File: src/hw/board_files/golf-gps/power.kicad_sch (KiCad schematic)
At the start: 19 parts, among them J3 USB_C_Receptacle_PowerOnly_6P, SW1 SW_SPDT, U2 MCP73831-2-OT, U3 TPS63031DSKR

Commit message: Added BOM file, finishing sch
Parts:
- added F1: 500mA, symbol Device:Fuse_Small
- renumbered C14 to C4, C15 to C5, C5 to C6, C6 to C7, C7 to C8, C1 to C9, D3 to D2, R7 to R5, R8 to R6, R9 to R7, R10 to R8
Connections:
- net VBAT: now also BT2.1 (+), F1.1
- net V_BCKP: now reaches D1.3 (A)
- net V_LiPo: no longer names the net of SW1.1 (B)
- net V_LiPo: now also F1.2; no longer BT2.1 (+)
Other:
- note added: "LiPo Battery Charger"
- note added: "Power"
- note removed: "Add fuse"
- note removed: "LiPo Charger"
- company: (none) -> Brady Kuhn
- title: (none) -> Golf GPS
- moved on the sheet: BT1, BT2, C4, C5, C6, C7, C8, C9, D1, D2, J3, L1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

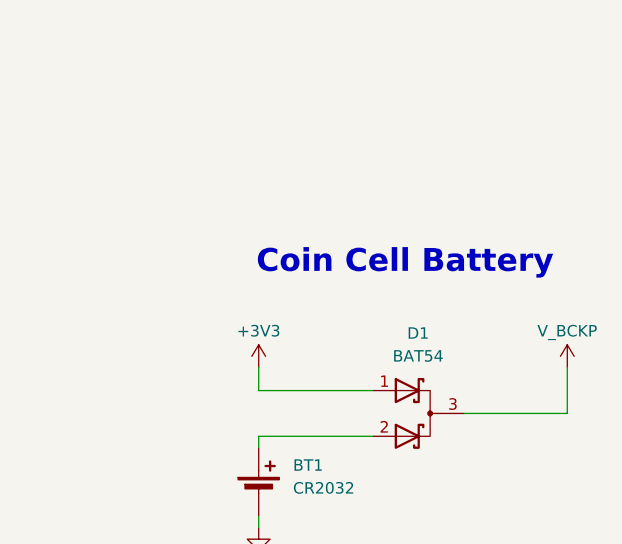
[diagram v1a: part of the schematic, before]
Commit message: Added PI filter to antenna.
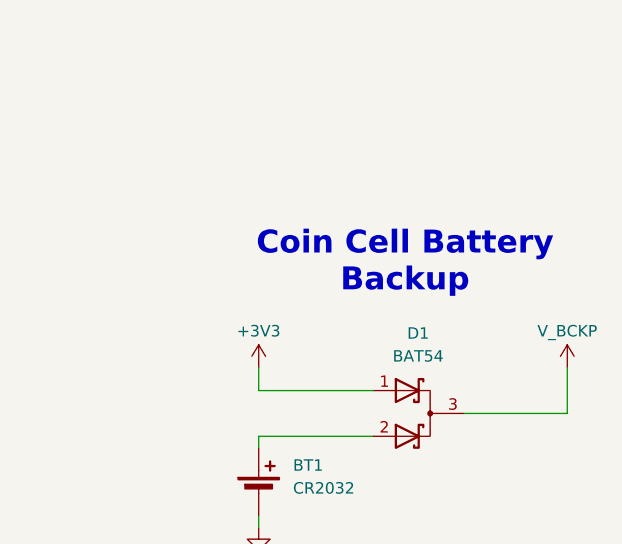
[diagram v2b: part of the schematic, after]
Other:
- note added: "Coin Cell Battery Backup"
- note removed: "Coin Cell Battery"
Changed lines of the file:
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@@
 		)
 	)
-	(text "Coin Cell Battery"
+	(text "Coin Cell Battery\nBackup"
 		(exclude_from_sim no)
 		(at 214.376 40.386 0)

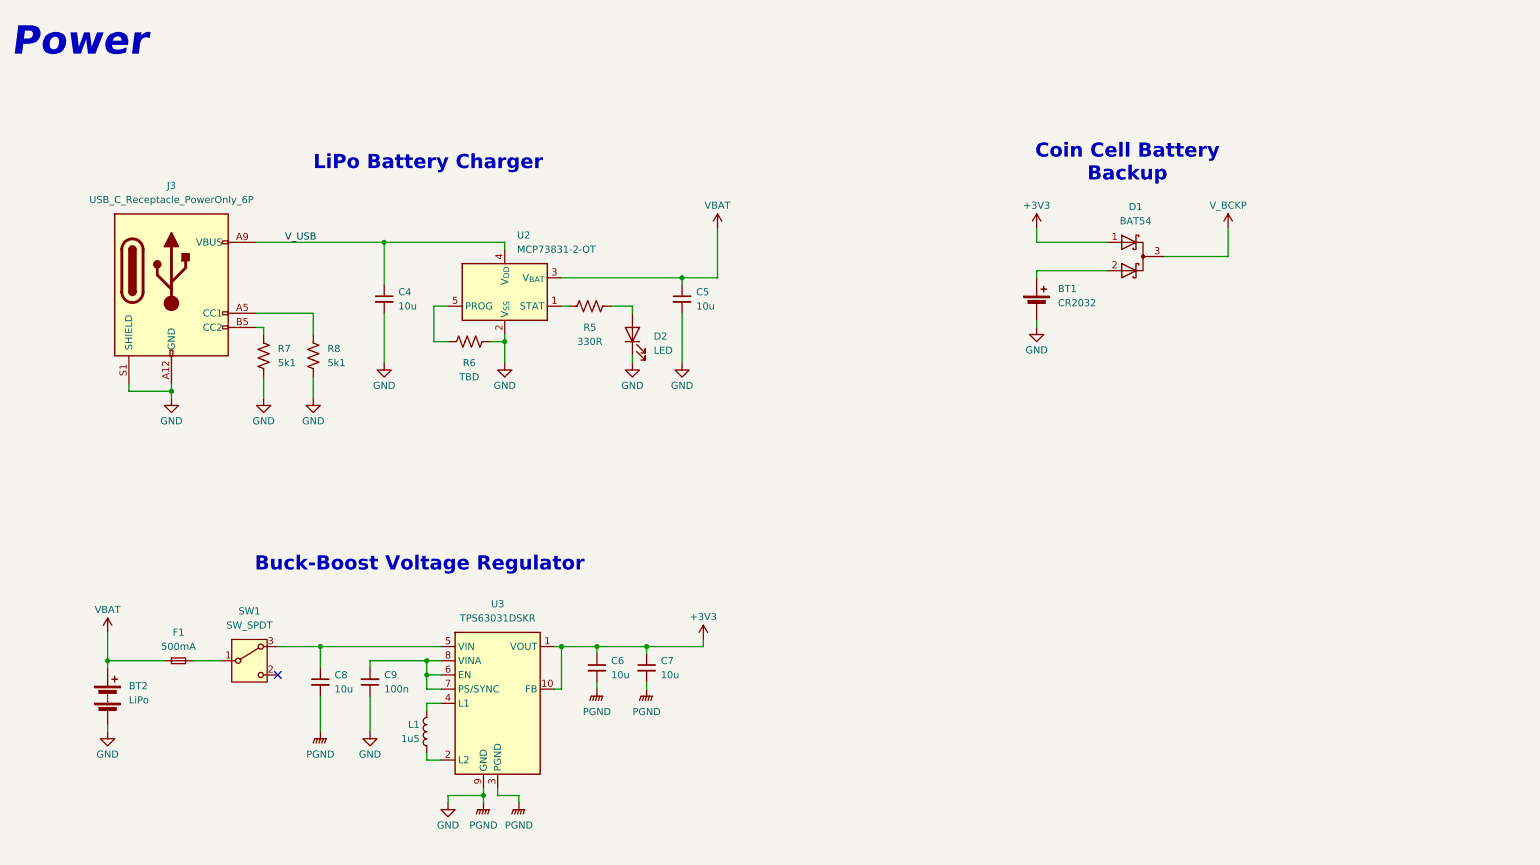
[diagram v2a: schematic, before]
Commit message: Finished sch, started power section on PCB
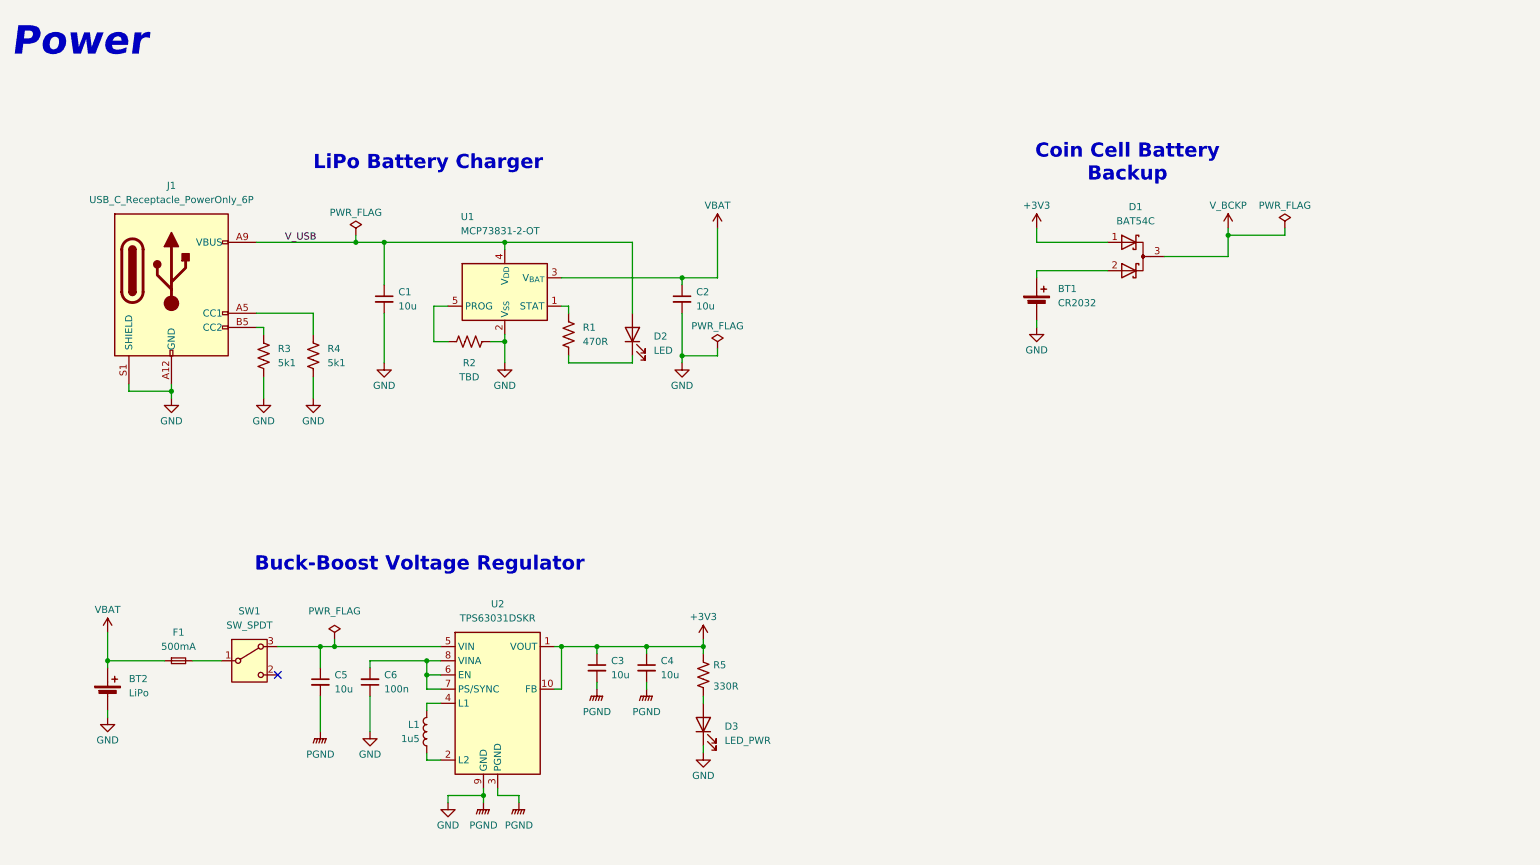
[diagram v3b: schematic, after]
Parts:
- removed BT2: LiPo, symbol Device:Battery
- added BT2: LiPo, Connector_JST:JST_PH_S2B-PH-K_1x02_P2.00mm_Horizontal, symbol Device:Battery_Cell
- added D3: LED_PWR, LED_SMD:LED_0805_2012Metric, symbol Device:LED
- added R5: 330R, Resistor_SMD:R_0603_1608Metric, symbol Device:R_US
- BT1: footprint (none) -> Battery:BatteryHolder_Multicomp_BC-2001_1x2032
- C1: renamed from C4; footprint (none) -> Capacitor_SMD:C_0805_2012Metric
- C2: renamed from C5; footprint (none) -> Capacitor_SMD:C_0805_2012Metric
- C3: renamed from C6; footprint (none) -> Capacitor_SMD:C_0603_1608Metric
- C4: renamed from C7; footprint (none) -> Capacitor_SMD:C_0603_1608Metric
- C5: renamed from C8; footprint (none) -> Capacitor_SMD:C_0603_1608Metric
- C6: renamed from C9; footprint (none) -> Capacitor_SMD:C_0603_1608Metric
- D1: value BAT54 -> BAT54C; footprint (none) -> Package_TO_SOT_SMD:SOT-23-3
- D2: footprint (none) -> LED_SMD:LED_0603_1608Metric
- F1: footprint (none) -> Fuse:Fuse_1812_4532Metric
- J1: renamed from J3; footprint (none) -> Connector_USB:USB_C_Receptacle_GCT_USB4125-xx-x-0190_6P_TopMnt_Horizontal
- R1: renamed from R5; value 330R -> 470R; footprint (none) -> Resistor_SMD:R_0603_1608Metric
- R2: renamed from R6; footprint (none) -> Resistor_SMD:R_0603_1608Metric
- R3: renamed from R7; footprint (none) -> Resistor_SMD:R_0603_1608Metric
- R4: renamed from R8; footprint (none) -> Resistor_SMD:R_0603_1608Metric
- renumbered U2 to U1, U3 to U2
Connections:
- net +3V3: now also R5.1
- net GND: now also BT2.2 (-), D3.1 (K); no longer D2.1 (K)
- net VBAT: now also BT2.1 (+)
- net V_USB: now also D2.2 (A)
- net at R1.2: now also U1.1 (STAT); no longer D2.2 (A)
- net at R1.1: now also D2.1 (K); no longer U1.1 (STAT)
- new net: D3.2 (A), R5.2
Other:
- company: Brady Kuhn -> B. Kuhn
- moved on the sheet: R1

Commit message: PCB Progress
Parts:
- BT1: footprint Battery:BatteryHolder_Multicomp_BC-2001_1x2032 -> Battery:BatteryHolder_Keystone_3034_1x20mm
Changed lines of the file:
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@@
 			)
 		)
-		(property "Footprint" "Battery:BatteryHolder_Multicomp_BC-2001_1x2032"
+		(property "Footprint" "Battery:BatteryHolder_Keystone_3034_1x20mm"
 			(at 198.12 64.516 90)
 			(effects

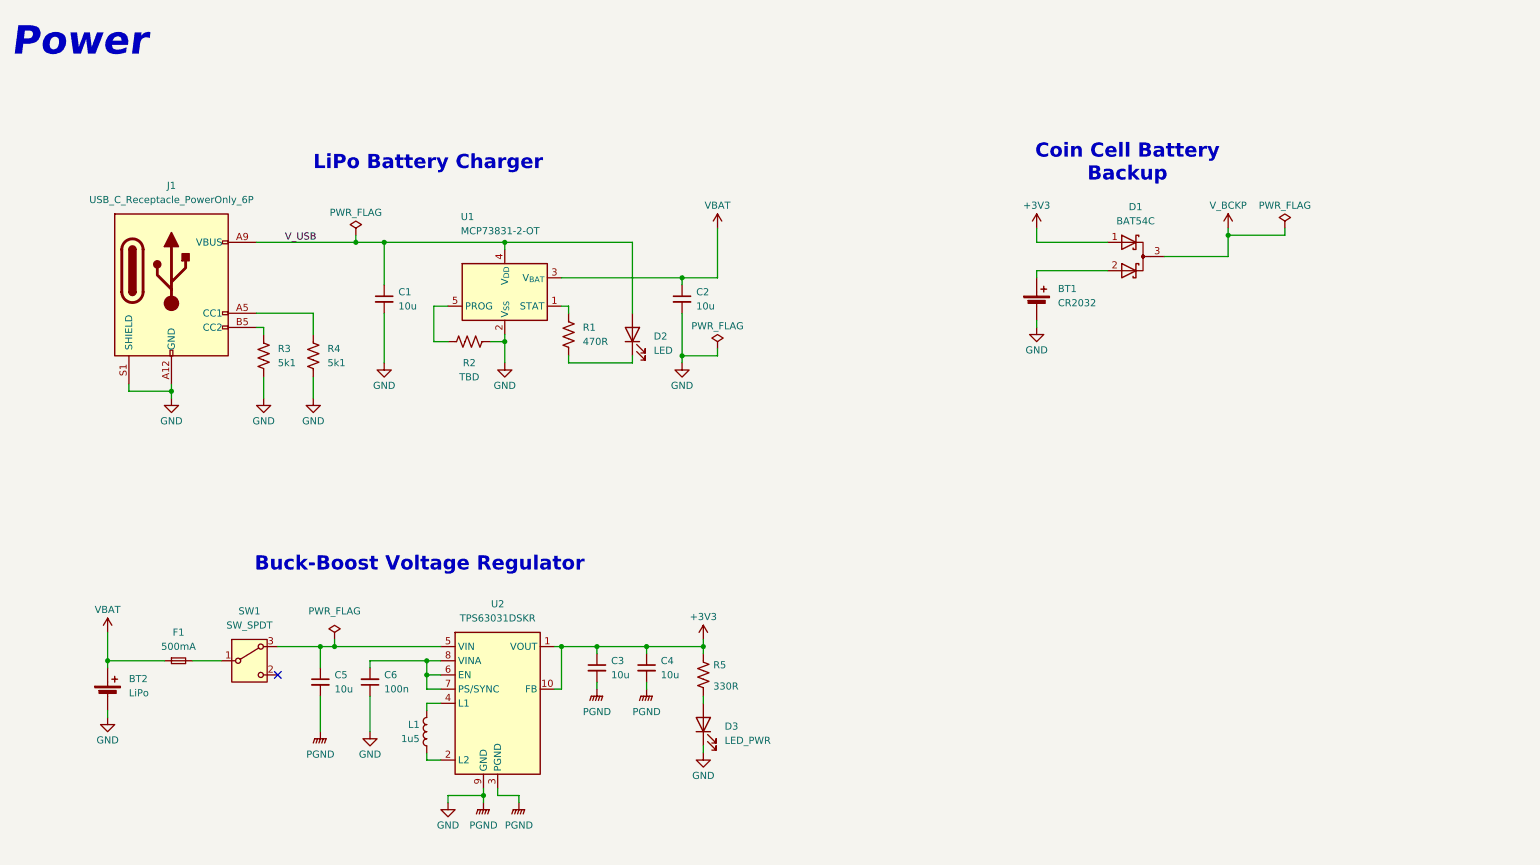
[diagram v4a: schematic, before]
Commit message: Added USBC to UART bridge for programming. Changed pinout. Added pinout spreadsheet in docs.
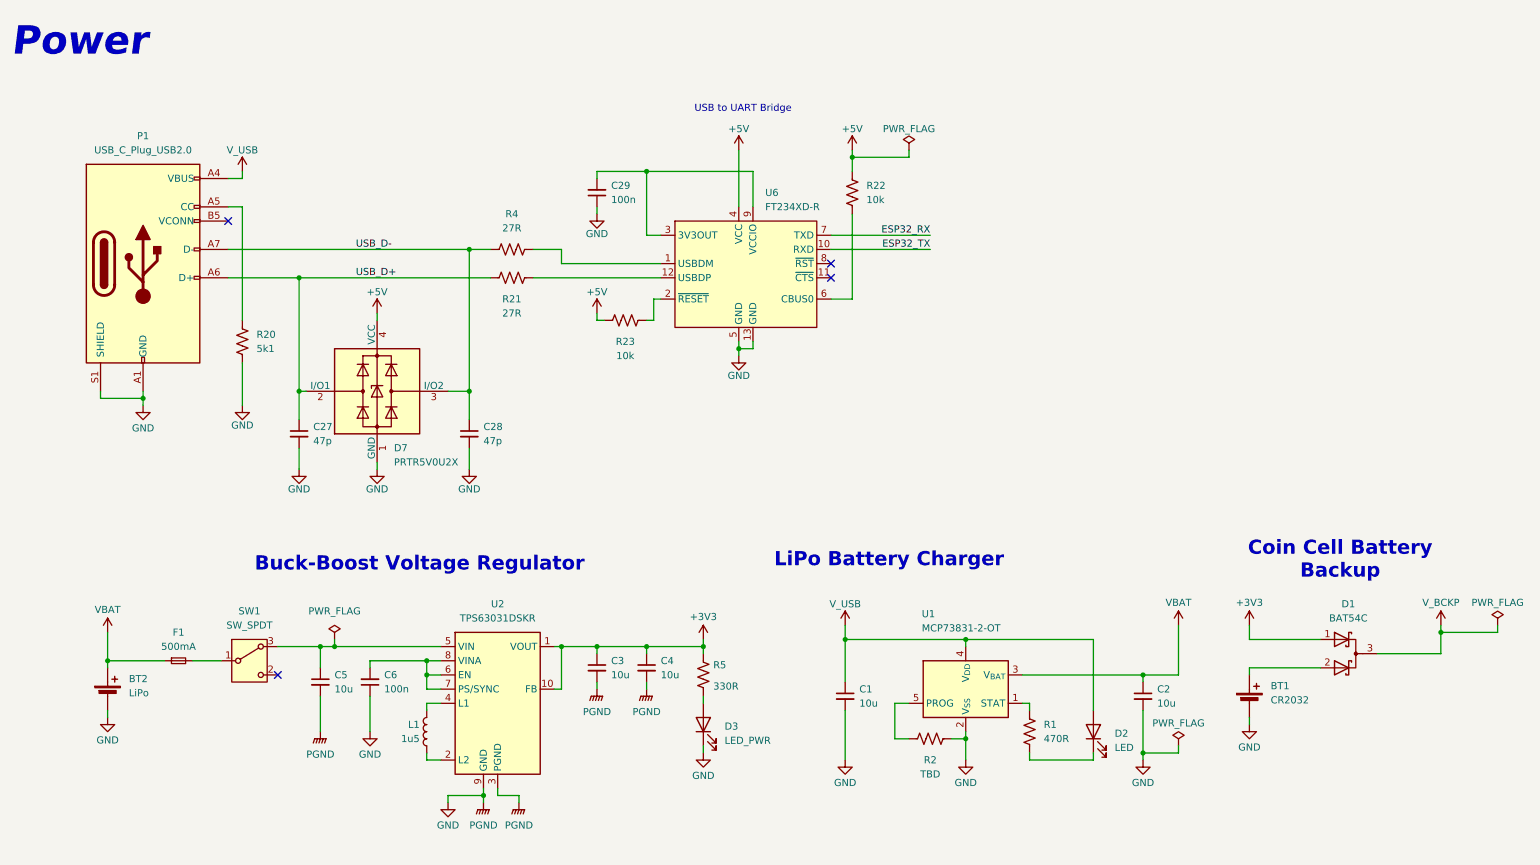
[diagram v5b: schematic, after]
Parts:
- removed J1: USB_C_Receptacle_PowerOnly_6P, Connector_USB:USB_C_Receptacle_GCT_USB4125-xx-x-0190_6P_TopMnt_Horizontal, symbol Connector:USB_C_Receptacle_PowerOnly_6P
- removed R3: 5k1, Resistor_SMD:R_0603_1608Metric, symbol Device:R_US
- added C27, C28: 47p, Capacitor_SMD:C_0603_1608Metric, symbol Device:C_Small
- added C29: 100n, Capacitor_SMD:C_0603_1608Metric, symbol Device:C_Small
- added D7: PRTR5V0U2X, Package_TO_SOT_SMD:SOT-143, symbol Power_Protection:PRTR5V0U2X
- added P1: USB_C_Plug_USB2.0, symbol Connector:USB_C_Plug_USB2.0
- added R20: 5k1, Resistor_SMD:R_0603_1608Metric, symbol Device:R_US
- added R21: 27R, Resistor_SMD:R_0603_1608Metric, symbol Device:R_US
- added R22, R23: 10k, Resistor_SMD:R_0603_1608Metric, symbol Device:R_US
- added U6: FT234XD-R, Package_DFN_QFN:DFN-12-1EP_3x3mm_P0.45mm_EP1.65x2.38mm, symbol smart_clock:FT234XD-R
- R4: value 5k1 -> 27R; LCSC (none) -> C25190
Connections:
- net GND: now also C27.2, C28.2, C29.1, D7.1 (GND), P1.A1 (GND), P1.A12 (GND), P1.B1 (GND), P1.B12 (GND), P1.S1 (SHIELD), R20.1, U6.13 (GND), U6.5 (GND); no longer R4.2
- net V_USB: now also P1.A4 (VBUS), P1.A9 (VBUS), P1.B4 (VBUS), P1.B9 (VBUS)
- net USB_D-: now reaches R4.1
- net USB_D-: now also C28.1, D7.3 (I/O2), P1.A7 (D-)
- new net: P1.A5 (CC), R20.2
- new net: R23.1, U6.2 (~{RESET})
- new net: R22.2, U6.6 (CBUS0)
- new net: R4.2, U6.1 (USBDM)
- new net: R21.2, U6.12 (USBDP)
- new net: C29.2, U6.3 (3V3OUT), U6.9 (VCCIO)
- new net +5V: D7.4 (VCC), R22.1, R23.2, U6.4 (VCC)
- new net ESP32_RX: U6.7 (TXD)
- new net ESP32_TX: U6.10 (RXD)
- new net USB_D+: C27.1, D7.2 (I/O1), P1.A6 (D+), R21.1
- no-connect marks 1 -> 4
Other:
- note added: "USB to UART Bridge"
- moved on the sheet: BT1, C1, C2, D1, D2, R1, R2, U1

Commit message: Finished new sch. Updated pinout. Started new PCB.
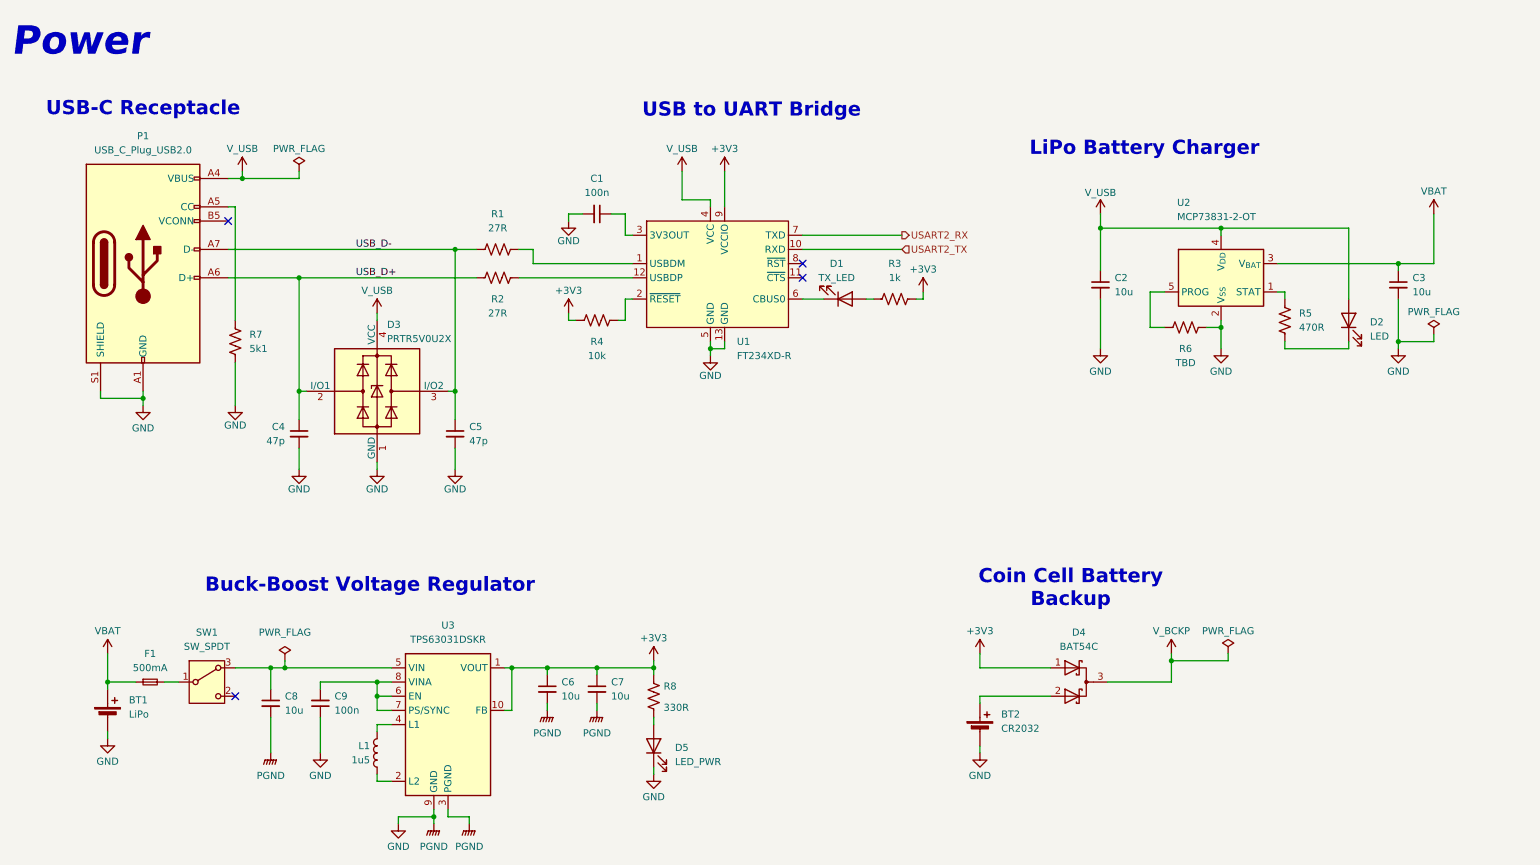
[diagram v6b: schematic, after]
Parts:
- added D1: TX_LED, LED_SMD:LED_0603_1608Metric, symbol Device:LED
- C2: renamed from C1; footprint Capacitor_SMD:C_0805_2012Metric -> Capacitor_SMD:C_0603_1608Metric
- C3: renamed from C2; footprint Capacitor_SMD:C_0805_2012Metric -> Capacitor_SMD:C_0603_1608Metric
- P1: footprint (none) -> Connector_USB:USB_C_Receptacle_GCT_USB4110
- R3: renamed from R22; value 10k -> 1k
- renumbered BT2 to BT1, BT1 to BT2, C29 to C1, C27 to C4, C28 to C5, C3 to C6, C4 to C7, C5 to C8, C6 to C9, D7 to D3, D1 to D4, D3 to D5, R4 to R1, R21 to R2, R23 to R4, R1 to R5, R2 to R6, R20 to R7, R5 to R8, U6 to U1, U1 to U2, U2 to U3
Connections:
- net +3V3: now also R3.2, R4.2, U1.9 (VCCIO)
- net GND: now also C1.2; no longer C1.1
- net V_USB: now also D3.4 (VCC), U1.4 (VCC)
- net at U1.6 (CBUS0): now also D1.1 (K); no longer R3.2
- removed net +5V: D3.4 (VCC), R3.1, R4.2, U1.4 (VCC)
- net ESP32_RX renamed USART2_RX
- net ESP32_TX renamed USART2_TX
- new net: D1.2 (A), R3.1
- new net: C1.1, U1.3 (3V3OUT)
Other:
- note added: "USB-C Receptacle"
- moved on the sheet: BT1, BT2, C1, C2, C3, C5, C6, C7, C8, C9, D2, D4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
